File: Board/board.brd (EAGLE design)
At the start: 68.6 x 53.3 mm, 4 parts, among them IC1 L293D

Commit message: various stuff and board
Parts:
- removed R1, R2: (no value), adafruit:0204/5
- added ALIM, BUZZ, MOT1, MOT2: (no value), pinhead:1X02
- added PHOTO: (no value), pinhead:2X03
- added R3: 10k, BaseApp:R0603
- added S1, S3, SW1, SW2, SW3: (no value), adafruit:B3F-40XX
- added SRVO, ULTRA: (no value), pinhead:1X03
- moved IC1 12.5 mm to (48.3, 41.9)
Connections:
- removed net GND1: IC1.4
- removed net GND2: IC1.5
- removed net GND3: IC1.13
- removed net GND4: IC1.12
- removed net VCC1: IC1.16
- removed net VCC2: IC1.8
- new net N$1: IC1.3, MOT1.2
- new net N$10: IC1.1, PCB1.11
- new net N$11: PCB1.A1, PHOTO.6
- new net N$12: PCB1.A0, PHOTO.4
- new net N$13: PHOTO.2
- new net N$14: PCB1.6, SRVO.2
- new net N$15: PCB1.3, ULTRA.2
- new net N$16: BUZZ.1, PCB1.5
- new net N$17: PCB1.7, SW3.3
- new net N$18: R3.2, SW3.4
- new net N$19: PCB1.4, SW2.3
- new net N$2: IC1.6, MOT1.1
- new net N$3: IC1.11, MOT2.2
- new net N$4: IC1.14, MOT2.1
- new net N$5: IC1.2, PCB1.12
- new net N$6: IC1.7, PCB1.13
- new net N$7: IC1.15, PCB1.10
- new net N$8: IC1.9, PCB1.9
- new net N$9: IC1.10, PCB1.8
- net +5V: now also ALIM.2, IC1.16, IC1.8, PHOTO.1, PHOTO.3, PHOTO.5, SRVO.1, SW1.1, SW2.2, SW3.1, ULTRA.1
- net GND: now also ALIM.1, BUZZ.2, IC1.12, IC1.13, IC1.4, IC1.5, PCB1.SCL, R3.1, SRVO.3, ULTRA.3; no longer PCB1.GND

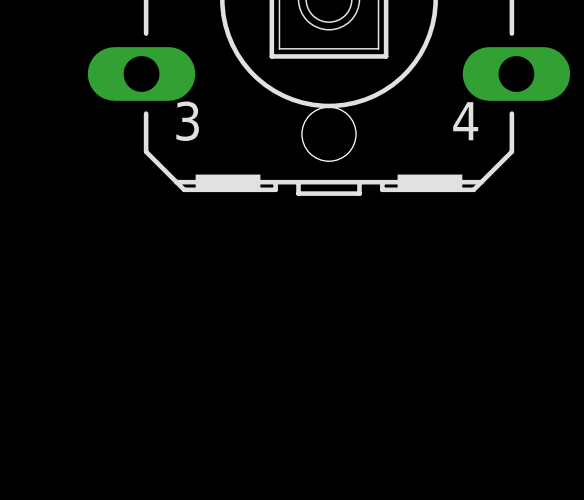
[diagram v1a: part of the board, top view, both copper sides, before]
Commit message: Eagle : Switches connected, useless backups deleted
- Connected the switches left unconnected last time
- Optimized the schematics
- Removed the now useless backups & libraries - only kept the 3 most
recent versions.
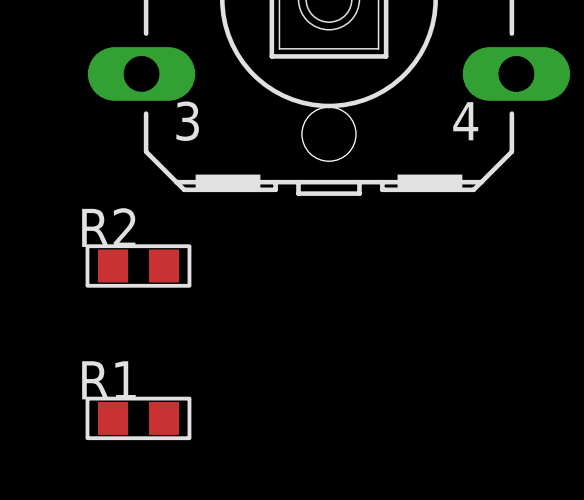
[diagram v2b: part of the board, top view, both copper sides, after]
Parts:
- added R1, R2: 10k, BaseApp:R0603
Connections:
- new net N$20: R2.2, SW2.4
- new net N$21: R1.2, SW1.4
- net GND: now also R1.1, R2.1
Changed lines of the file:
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@@
 <attribute name="OC_FARNELL" value="176434" x="-11.43" y="-85.09" size="1.778" layer="27" display="off"/>
 </element>
+<element name="R2" library="BaseApp" package="R0603" value="10k" x="-17.78" y="-93.98"/>
+<element name="R1" library="BaseApp" package="R0603" value="10k" x="-17.78" y="-99.06"/>
 </elements>
 <signals>
@@
 <contactref element="R3" pad="1"/>
 <contactref element="BUZZ" pad="2"/>
+<contactref element="R2" pad="1"/>
+<contactref element="R1" pad="1"/>
+<wire x1="-18.63" y1="-93.98" x2="-18.63" y2="-99.06" width="0" layer="19" extent="1-1"/>
+<wire x1="-18.63" y1="-59.69" x2="-18.63" y2="-93.98" width="0" layer="19" extent="1-1"/>
+<wire x1="-7.62" y1="-6.35" x2="-18.63" y2="-59.69" width="0" layer="19" extent="1-1"/>
+<wire x1="1.27" y1="-8.89" x2="-7.62" y2="-6.35" width="0" layer="19" extent="1-1"/>
+<wire x1="1.27" y1="-2.54" x2="1.27" y2="-8.89" width="0" layer="19" extent="1-1"/>
+<wire x1="-3.81" y1="5.08" x2="1.27" y2="-2.54" width="0" layer="19" extent="1-1"/>
+<wire x1="48.26" y1="7.62" x2="1.27" y2="-2.54" width="0" layer="19" extent="1-1"/>
+<wire x1="50.8" y1="7.62" x2="48.26" y2="7.62" width="0" layer="19" extent="1-1"/>
+<wire x1="49.53" y1="38.1" x2="48.26" y2="7.62" width="0" layer="19" extent="1-1"/>
+<wire x1="46.99" y1="38.1" x2="49.53" y2="38.1" width="0" layer="19" extent="1-1"/>
+<wire x1="49.53" y1="45.72" x2="49.53" y2="38.1" width="0" layer="19" extent="1-1"/>
 <wire x1="46.99" y1="45.72" x2="49.53" y2="45.72" width="0" layer="19" extent="1-1"/>
-<wire x1="49.53" y1="38.1" x2="49.53" y2="45.72" width="0" layer="19" extent="1-1"/>
-<wire x1="46.99" y1="38.1" x2="49.53" y2="38.1" width="0" layer="19" extent="1-1"/>
 <wire x1="26.416" y1="55.88" x2="46.99" y2="45.72" width="0" layer="19" extent="1-1"/>
-<wire x1="50.8" y1="7.62" x2="49.53" y2="38.1" width="0" layer="19" extent="1-1"/>
-<wire x1="48.26" y1="7.62" x2="50.8" y2="7.62" width="0" layer="19" extent="1-1"/>
-<wire x1="1.27" y1="-2.54" x2="48.26" y2="7.62" width="0" layer="19" extent="1-1"/>
-<wire x1="1.27" y1="-8.89" x2="1.27" y2="-2.54" width="0" layer="19" extent="1-1"/>
-<wire x1="-3.81" y1="5.08" x2="1.27" y2="-2.54" width="0" layer="19" extent="1-1"/>
-<wire x1="-7.62" y1="-6.35" x2="1.27" y2="-8.89" width="0" layer="19" extent="1-1"/>
-<wire x1="-18.63" y1="-59.69" x2="-7.62" y2="-6.35" width="0" layer="19" extent="1-1"/>
 </signal>
 <signal name="+5V">
@@
 <wire x1="-17.6784" y1="-87.5792" x2="60.96" y2="55.88" width="0" layer="19" extent="1-1"/>
 </signal>
+<signal name="N$20">
+<contactref element="SW2" pad="4"/>
+<contactref element="R2" pad="2"/>
+<wire x1="-5.1816" y1="-87.5792" x2="-16.93" y2="-93.98" width="0" layer="19" extent="1-1"/>
+</signal>
+<signal name="N$21">
+<contactref element="SW1" pad="4"/>
+<contactref element="R1" pad="2"/>
+<wire x1="-5.1816" y1="-72.3392" x2="-16.93" y2="-99.06" width="0" layer="19" extent="1-1"/>
+</signal>
 </signals>

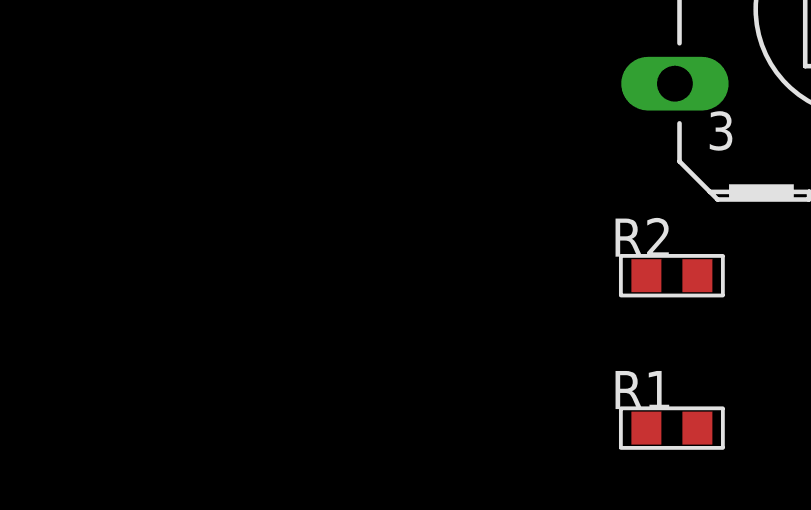
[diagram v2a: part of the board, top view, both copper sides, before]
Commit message: Eagle : Added thumbwheels
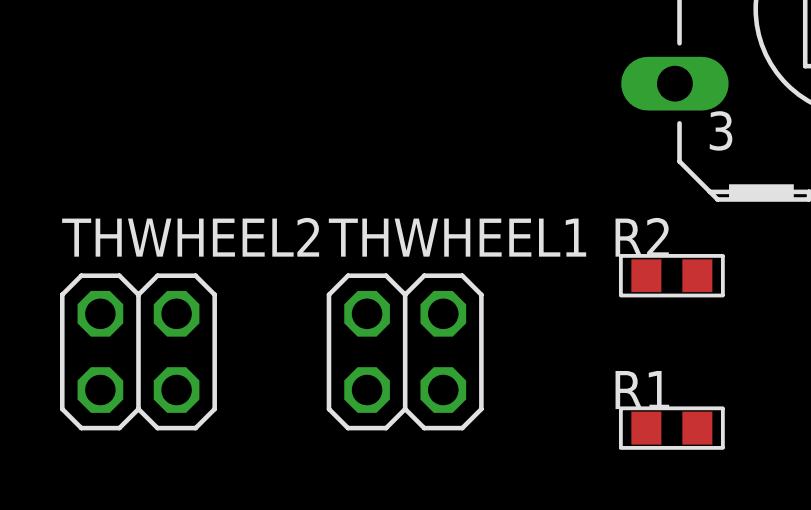
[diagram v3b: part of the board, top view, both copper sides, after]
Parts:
- added THWHEEL1, THWHEEL2: (no value), pinhead:2X02
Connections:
- new net N$22: PCB1.A2, THWHEEL1.4
- new net N$23: PCB1.A3, THWHEEL2.4
- net +5V: now also THWHEEL1.1, THWHEEL1.3, THWHEEL2.1, THWHEEL2.3
- net GND: now also THWHEEL1.2, THWHEEL2.2
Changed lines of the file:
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@@
 <element name="R2" library="BaseApp" package="R0603" value="10k" x="-17.78" y="-93.98"/>
 <element name="R1" library="BaseApp" package="R0603" value="10k" x="-17.78" y="-99.06"/>
+<element name="THWHEEL1" library="pinhead" package="2X02" value="" x="-26.67" y="-96.52"/>
+<element name="THWHEEL2" library="pinhead" package="2X02" value="" x="-35.56" y="-96.52"/>
 </elements>
 <signals>
@@
 <contactref element="R2" pad="1"/>
 <contactref element="R1" pad="1"/>
-<wire x1="-18.63" y1="-93.98" x2="-18.63" y2="-99.06" width="0" layer="19" extent="1-1"/>
+<contactref element="THWHEEL2" pad="2"/>
+<contactref element="THWHEEL1" pad="2"/>
+<wire x1="-27.94" y1="-95.25" x2="-36.83" y2="-95.25" width="0" layer="19" extent="1-1"/>
+<wire x1="-18.63" y1="-93.98" x2="-27.94" y2="-95.25" width="0" layer="19" extent="1-1"/>
+<wire x1="-18.63" y1="-99.06" x2="-18.63" y2="-93.98" width="0" layer="19" extent="1-1"/>
 <wire x1="-18.63" y1="-59.69" x2="-18.63" y2="-93.98" width="0" layer="19" extent="1-1"/>
 <wire x1="-7.62" y1="-6.35" x2="-18.63" y2="-59.69" width="0" layer="19" extent="1-1"/>
@@
 <contactref element="SW1" pad="1"/>
 <contactref element="SW2" pad="2"/>
+<contactref element="THWHEEL1" pad="1"/>
+<contactref element="THWHEEL1" pad="3"/>
+<contactref element="THWHEEL2" pad="1"/>
+<contactref element="THWHEEL2" pad="3"/>
+<wire x1="-34.29" y1="-97.79" x2="-36.83" y2="-97.79" width="0" layer="19" extent="1-1"/>
+<wire x1="-27.94" y1="-97.79" x2="-34.29" y2="-97.79" width="0" layer="19" extent="1-1"/>
+<wire x1="-25.4" y1="-97.79" x2="-27.94" y2="-97.79" width="0" layer="19" extent="1-1"/>
+<wire x1="-5.1816" y1="-82.6008" x2="-25.4" y2="-97.79" width="0" layer="19" extent="1-1"/>
+<wire x1="-17.6784" y1="-67.3608" x2="-5.1816" y2="-82.6008" width="0" layer="19" extent="1-1"/>
+<wire x1="-17.6784" y1="-33.0708" x2="-17.6784" y2="-67.3608" width="0" layer="19" extent="1-1"/>
+<wire x1="-16.51" y1="-6.35" x2="-17.6784" y2="-33.0708" width="0" layer="19" extent="1-1"/>
+<wire x1="-19.05" y1="-6.35" x2="-16.51" y2="-6.35" width="0" layer="19" extent="1-1"/>
+<wire x1="-13.97" y1="-6.35" x2="-16.51" y2="-6.35" width="0" layer="19" extent="1-1"/>
+<wire x1="-3.81" y1="-8.89" x2="-13.97" y2="-6.35" width="0" layer="19" extent="1-1"/>
+<wire x1="-3.81" y1="-2.54" x2="-3.81" y2="-8.89" width="0" layer="19" extent="1-1"/>
+<wire x1="-1.27" y1="5.08" x2="-3.81" y2="-2.54" width="0" layer="19" extent="1-1"/>
+<wire x1="45.72" y1="7.62" x2="-1.27" y2="5.08" width="0" layer="19" extent="1-1"/>
+<wire x1="57.15" y1="38.1" x2="45.72" y2="7.62" width="0" layer="19" extent="1-1"/>
 <wire x1="39.37" y1="45.72" x2="57.15" y2="38.1" width="0" layer="19" extent="1-1"/>
-<wire x1="45.72" y1="7.62" x2="57.15" y2="38.1" width="0" layer="19" extent="1-1"/>
-<wire x1="-1.27" y1="5.08" x2="45.72" y2="7.62" width="0" layer="19" extent="1-1"/>
-<wire x1="-3.81" y1="-2.54" x2="-1.27" y2="5.08" width="0" layer="19" extent="1-1"/>
-<wire x1="-3.81" y1="-8.89" x2="-3.81" y2="-2.54" width="0" layer="19" extent="1-1"/>
-<wire x1="-13.97" y1="-6.35" x2="-3.81" y2="-8.89" width="0" layer="19" extent="1-1"/>
-<wire x1="-16.51" y1="-6.35" x2="-13.97" y2="-6.35" width="0" layer="19" extent="1-1"/>
-<wire x1="-19.05" y1="-6.35" x2="-16.51" y2="-6.35" width="0" layer="19" extent="1-1"/>
-<wire x1="-17.6784" y1="-33.0708" x2="-16.51" y2="-6.35" width="0" layer="19" extent="1-1"/>
-<wire x1="-17.6784" y1="-67.3608" x2="-17.6784" y2="-33.0708" width="0" layer="19" extent="1-1"/>
-<wire x1="-5.1816" y1="-82.6008" x2="-17.6784" y2="-67.3608" width="0" layer="19" extent="1-1"/>
 </signal>
 <signal name="N$5">
@@
 <wire x1="-5.1816" y1="-72.3392" x2="-16.93" y2="-99.06" width="0" layer="19" extent="1-1"/>
 </signal>
+<signal name="N$22">
+<contactref element="THWHEEL1" pad="4"/>
+<contactref element="PCB1" pad="A2"/>
+<wire x1="63.5" y1="7.62" x2="-25.4" y2="-95.25" width="0" layer="19" extent="1-1"/>
+</signal>
+<signal name="N$23">
+<contactref element="PCB1" pad="A3"/>
+<contactref element="THWHEEL2" pad="4"/>
+<wire x1="66.04" y1="7.62" x2="-34.29" y2="-95.25" width="0" layer="19" extent="1-1"/>
+</signal>
 </signals>

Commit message: Finished, and autorouted everything on 2 layers.
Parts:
- removed MOT1, MOT2: (no value), pinhead:1X02
- removed S1, S3: (no value), adafruit:B3F-40XX
- added MOT11, MOT12, MOT21, MOT22: (no value), pinhead:1X01
- moved THWHEEL2 154.6 mm to (68.6, 17.8)
- moved THWHEEL1 144.0 mm to (61.0, 17.8)
- moved R1 143.7 mm to (47.0, 29.2), turned to 90 degrees
- moved SW1 121.9 mm to (59.7, 29.2), turned to 180 degrees
- moved R2 112.6 mm to (27.9, 8.89)
- moved SW2 111.3 mm to (27.9, 19.1), turned to 270 degrees
- moved R3 111.0 mm to (43.2, 33.0), turned to 180 degrees
- moved SW3 98.8 mm to (48.3, 43.2), turned to 270 degrees
- moved ULTRA 92.2 mm to (71.1, 48.3), turned to 90 degrees
- moved BUZZ 90.9 mm to (64.8, 47.0), turned to 270 degrees
- moved SRVO 78.4 mm to (58.4, 48.3), turned to 90 degrees
- moved PHOTO 72.3 mm to (52.1, 17.8)
- moved ALIM 49.9 mm to (47.0, 11.4)
- moved IC1 19.0 mm to (29.2, 41.9)
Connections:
- new net N$24: PCB1.2, SW1.3
- net N$1: now also MOT11.1; no longer MOT1.2
- net N$2: now also MOT12.1; no longer MOT1.1
- net N$3: now also IC1.14, MOT21.1; no longer IC1.11, MOT2.2
- net N$4: now also IC1.11, MOT22.1; no longer IC1.14, MOT2.1

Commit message: Updated boad
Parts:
- removed BUZZ: (no value), pinhead:1X02
- removed PCB1: ARDUINO_UNO, E14_Arduino_revB:ARDUINO_UNO
- removed PHOTO: (no value), pinhead:2X03
- removed SRVO, ULTRA: (no value), pinhead:1X03
- removed SW1, SW2, SW3: (no value), adafruit:B3F-40XX
- removed THWHEEL1, THWHEEL2: (no value), pinhead:2X02
- added BUZ, PHS-L, WHL1, WHL2: (no value), pinhead:1X02
- added PHS-R: (no value), pinhead:2X02
- added R4, R5: 10k, resistor:R1206
- added R6: 220, resistor:R1206
- added S1, S2, S3: (no value), switch-omron:B3F-10XX
- added SND: (no value), pinhead:1X03
- added SRV: (no value), pinhead:1X03/90
- added U1: ARDUINOR3-BPLACE, adafruit:ARDUINOR3-BPLACE
- ALIM: value (none) -> 5V
- R1, R2, R3: device BaseApp:R0603 -> resistor:R1206
- moved R2 43.9 mm to (65.4, 31.8), flipped to the bottom, turned to 90 degrees
- moved R3 39.6 mm to (39.4, 72.4), flipped to the bottom
- moved R1 32.0 mm to (78.7, 33.0), flipped to the bottom
- moved MOT11 14.0 mm to (26.7, 19.1)
- moved MOT12 14.0 mm to (31.8, 19.1)
- moved IC1 11.5 mm to (27.9, 30.5)
- moved MOT22 10.9 mm to (31.8, 38.7)
- moved MOT21 9.71 mm to (27.3, 40.0)
- moved ALIM 9.16 mm to (54.6, 16.5), turned to 180 degrees
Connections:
- removed net N$15: PCB1.3, ULTRA.2
- removed net N$17: PCB1.7, SW3.3
- new net 3V: U1.3V
- new net PIN12: IC1.2, U1.D12
- new net PIN13: IC1.7, U1.D13
- new net VIN: U1.VIN
- net +5V: now also PHS-R.1, PHS-R.3, R6.2, S1.1, S2.2, S3.2, SND.2, SRV.2, U1.5V, WHL1.2, WHL2.2; no longer PCB1.5V, PHOTO.1, PHOTO.3, PHOTO.5, SRVO.1, SW1.1, SW2.2, SW3.1, THWHEEL1.1, THWHEEL1.3, THWHEEL2.1, THWHEEL2.3, ULTRA.1
- net GND: now also BUZ.2, PHS-L.2, R4.1, R5.2, SND.3, SRV.3, U1.GND, U1.GND1, U1.GND2; no longer BUZZ.2, PCB1.GND., PCB1.GND.., PCB1.SCL, SRVO.3, THWHEEL1.2, THWHEEL2.2, ULTRA.3
- net N$10: now also U1.D11; no longer PCB1.11
- net N$11: now also R4.2, U1.A2, WHL1.1; no longer PCB1.A1, PHOTO.6
- net N$12: now also PHS-L.1, R6.1; no longer PCB1.A0, PHOTO.4
- net N$13: now also R5.1, U1.A3, WHL2.1; no longer PHOTO.2
- net N$14: now also SRV.1, U1.D7; no longer PCB1.6, SRVO.2
- net N$16: now also BUZ.1, U1.D6; no longer BUZZ.1, PCB1.5
- net N$18: now also R2.2, S2.4; no longer R3.2, SW3.4
- net N$19: now also S3.3, U1.D4; no longer PCB1.4, SW2.3
- net N$20: now also R3.2, S3.4; no longer R2.2, SW2.4
- net N$21: now also S1.4; no longer SW1.4
- net N$22: now also SND.1, U1.D3; no longer PCB1.A2, THWHEEL1.4
- net N$23: now also S2.3, U1.D5; no longer PCB1.A3, THWHEEL2.4
- net N$24: now also S1.3, U1.D2; no longer PCB1.2, SW1.3
- net N$5: now also PHS-R.2, U1.A1; no longer IC1.2, PCB1.12
- net N$6: now also PHS-R.4, U1.A0; no longer IC1.7, PCB1.13
- net N$7: now also U1.D10; no longer PCB1.10
- net N$8: now also U1.D9; no longer PCB1.9
- net N$9: now also U1.D8; no longer PCB1.8
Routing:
- net +5V: track 0.00 -> 218.0 mm
- net N$10: track 0.00 -> 65.5 mm
- net PIN13: track 0.00 -> 63.7 mm
- net PIN12: track 0.00 -> 60.0 mm
- net N$7: track 0.00 -> 44.5 mm
- net GND: track 0.00 -> 42.2 mm
- net N$9: track 0.00 -> 38.6 mm
- net N$8: track 0.00 -> 31.4 mm
- net N$19: track 0.00 -> 26.6 mm
- net N$13: track 0.00 -> 18.6 mm
- net N$24: track 0.00 -> 15.4 mm
- net N$23: track 0.00 -> 13.4 mm
- net N$22: track 0.00 -> 13.3 mm
- net N$16: track 0.00 -> 11.7 mm
- net N$11: track 0.00 -> 10.5 mm
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- added copper zone on layer 16, net GND
- removed copper zone on layer 1, net GND
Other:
- board size 68.6 x 53.3 mm -> 78.7 x 73.7 mm
